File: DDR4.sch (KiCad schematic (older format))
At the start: 4 parts, among them U14 2199155-1

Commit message: Update labels on the schematics
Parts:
- removed R158: R_0R_0603, rdimm-breakout-footprints:0603-res, symbol rdimm-breakout:R_0R_0603-rdimm-breakout
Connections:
- net labels added: VCC2V5
- net labels removed: VDDSPD
- wire segments 409 -> 407
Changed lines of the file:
@@
 Text GLabel 11950 8225 2    50   Input ~ 0
 DQ59
-Text GLabel 11950 8425 2    50   Input ~ 0
-VDDSPD
 Wire Wire Line
 	11225 8425 11950 8425
@@
 Wire Wire Line
 	10225 8225 10225 9000
-Text GLabel 13975 9375 2    50   Input ~ 0
-VDDSPD
-Wire Wire Line
-	13400 9375 13100 9375
-Text GLabel 13100 9375 0    50   Input ~ 0
-VPP
-$Comp
-L rdimm-breakout:R_0R_0603-rdimm-breakout R?
-U 1 1 632B1D0D
-P 13550 9375
-AR Path="/60225B0C/632B1D0D" Ref="R?"  Part="1"
-AR Path="/61827943/632B1D0D" Ref="R158"  Part="1"
-F 0 "R158" H 13500 9475 60  0000 C CNN
-F 1 "R_0R_0603" H 13550 9225 60  0001 C CNN
-F 2 "rdimm-breakout-footprints:0603-res" H 13750 9575 60  0001 L CNN
-F 3 "" H 13550 9375 50  0001 C CNN
-F 4 "BOURNS" H 13750 9775 60  0001 L CNN "Manufacturer"
-F 5 "CR0603-J/-000ELF" H 13750 9675 60  0001 L CNN "MPN"
-F 6 "0R" H 13700 9325 50  0000 C CNN "Val"
-	1    13550 9375
-	1    0    0    -1
-$EndComp
-Wire Wire Line
-	13700 9375 13975 9375
 Text Notes 12325 8450 0    50   ~ 0
 2V5
@@
 Text GLabel 11950 8525 2    50   Input ~ 0
 SDA_2V5
+Text GLabel 11950 8425 2    50   Input ~ 0
+VCC2V5
 $EndSCHEMATC

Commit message: Add initial component placement
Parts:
- removed R157: R_0R_0603, rdimm-breakout-footprints:0603-res, symbol rdimm-breakout:R_0R_0603-rdimm-breakout
- removed TP10: TP_SMD1MM, rdimm-breakout-footprints:Testpoint_smd_1mm, symbol rdimm-breakout:TP_SMD1MM-rdimm-breakout
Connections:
- net labels removed: VIN
- wire segments 407 -> 405
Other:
- note removed: "NVRDIMM Backup voltage"
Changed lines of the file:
@@
 Wire Wire Line
 	5250 2050 4850 2050
-$Comp
-L rdimm-breakout:TP_SMD1MM-rdimm-breakout TP10
-U 1 1 618505E7
-P 2250 1850
-F 0 "TP10" V 2155 1897 50  0000 C CNN
-F 1 "TP_SMD1MM" H 2250 1750 50  0001 C CNN
-F 2 "rdimm-breakout-footprints:Testpoint_smd_1mm" H 2450 2050 60  0001 L CNN
-F 3 "" H 2450 2150 60  0001 L CNN
-	1    2250 1850
-	0    -1   -1   0
-$EndComp
-Text Label 2000 1850 0    50   ~ 0
-12V
-Wire Notes Line
-	1275 1550 1275 2050
-Wire Notes Line
-	1275 2050 2350 2050
-Wire Notes Line
-	2350 2050 2350 1550
-Wire Notes Line
-	2350 1550 1275 1550
-Text Notes 1350 1650 0    50   ~ 0
-NVRDIMM Backup voltage
-$Comp
-L rdimm-breakout:R_0R_0603-rdimm-breakout R157
-U 1 1 61903C55
-P 1800 1850
-F 0 "R157" H 1800 1950 60  0000 C CNN
-F 1 "R_0R_0603" H 1800 1700 60  0001 C CNN
-F 2 "rdimm-breakout-footprints:0603-res" H 2000 2050 60  0001 L CNN
-F 3 "" H 1800 1850 50  0001 C CNN
-F 4 "BOURNS" H 2000 2250 60  0001 L CNN "Manufacturer"
-F 5 "CR0603-J/-000ELF" H 2000 2150 60  0001 L CNN "MPN"
-F 6 "0R" H 1950 1775 50  0000 C CNN "Val"
-F 7 "DNP" H 1800 1850 50  0000 C CNN "DNP"
-	1    1800 1850
-	-1   0    0    1
-$EndComp
-Wire Wire Line
-	2150 1850 1950 1850
-Text GLabel 1550 1850 0    50   Input ~ 0
-VIN
-Wire Wire Line
-	1650 1850 1550 1850
 Text GLabel 3500 2050 0    50   Input ~ 0
 NC

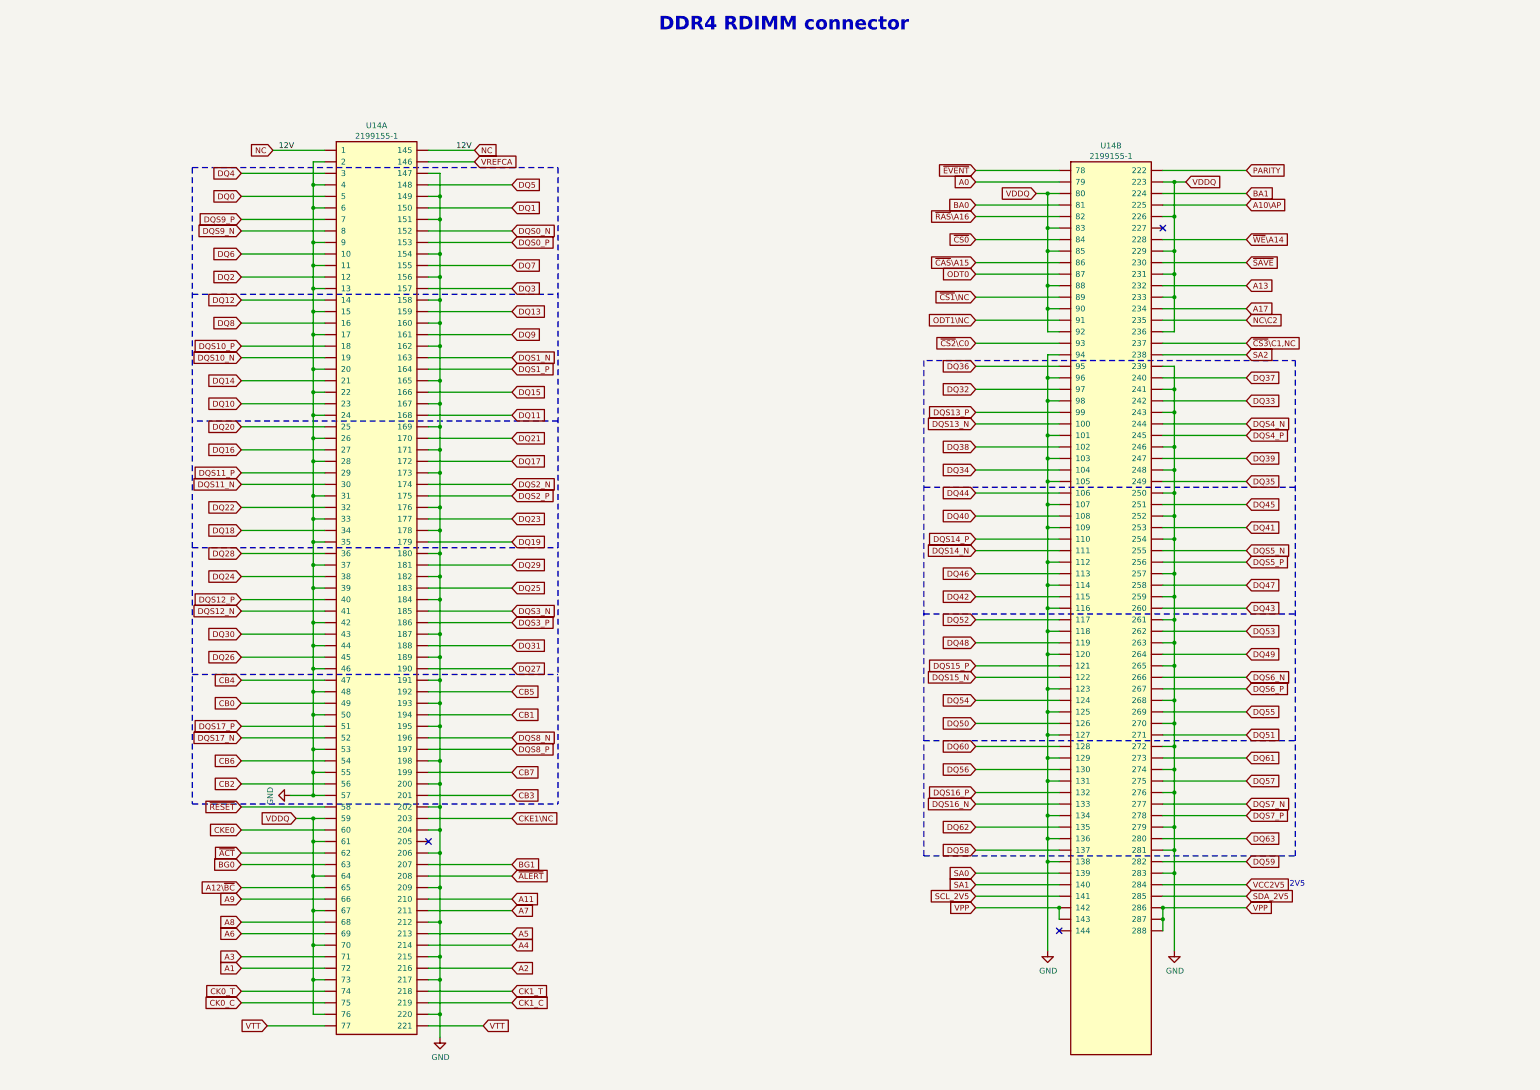
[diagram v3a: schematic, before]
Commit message: Assign MPN to the RDIMM connector
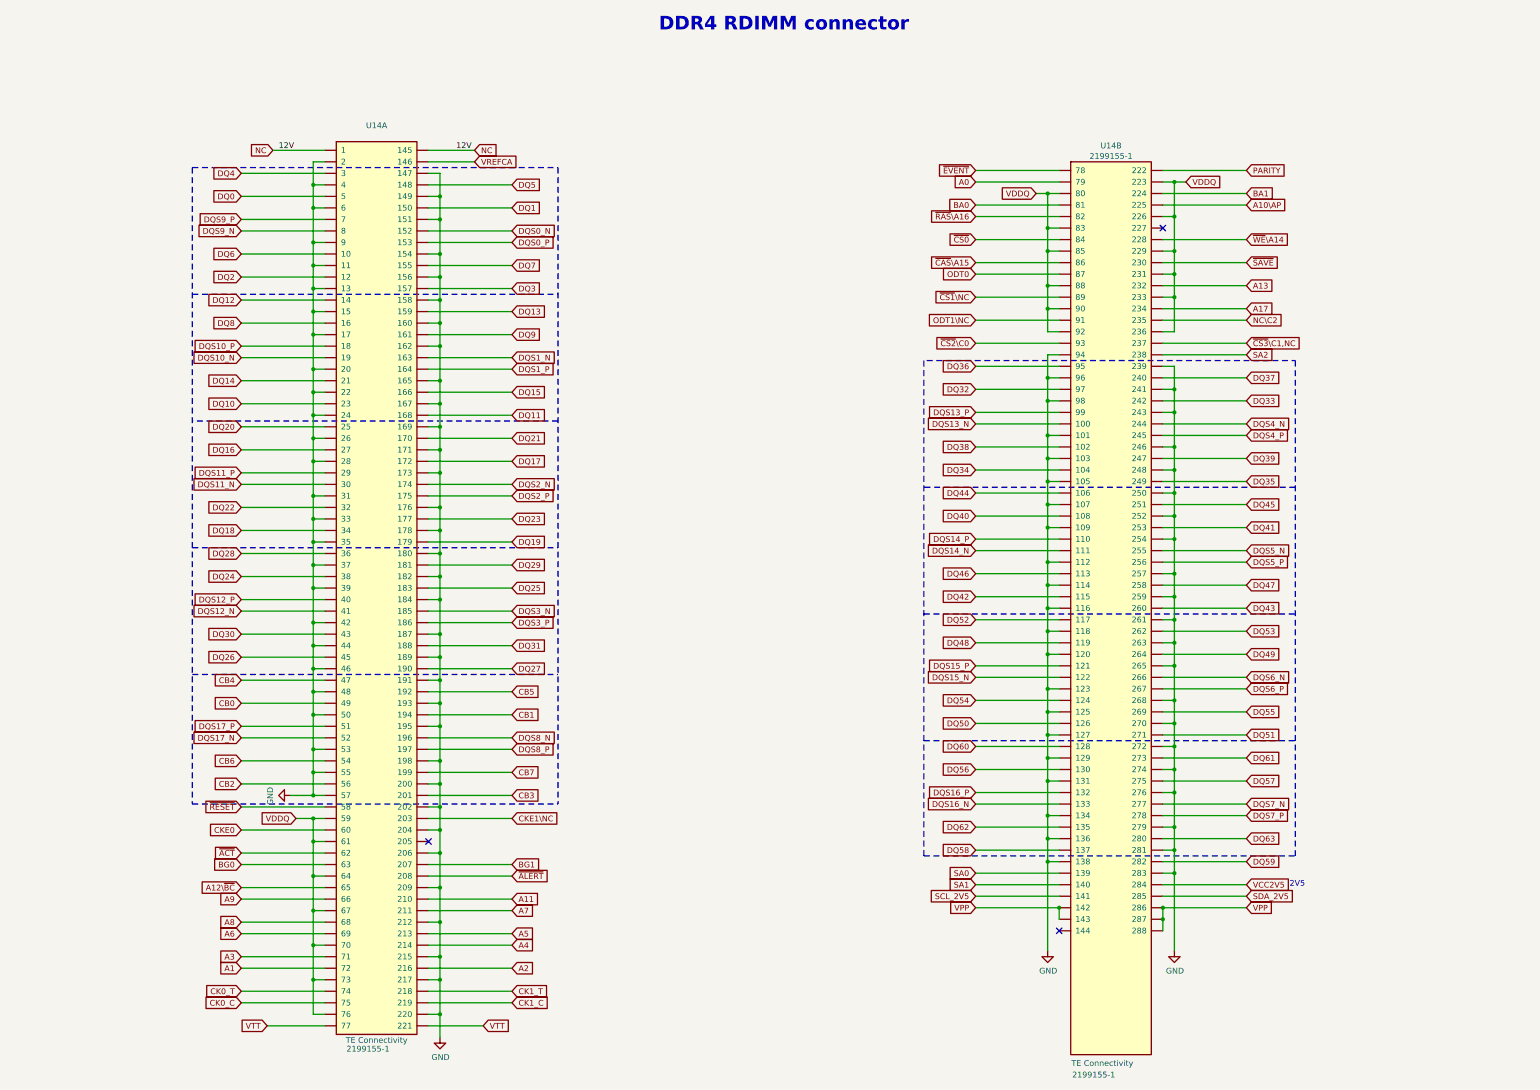
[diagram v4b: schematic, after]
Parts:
- U14: MPN (none) -> 2199155-1; Manufacturer (none) -> TE Connectivity
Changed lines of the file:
@@
 F 1 "2199155-1" H 10775 17649 50  0000 C CNN
 F 2 "rdimm-breakout-footprints:2199155-1" H 9500 16575 50  0001 C CNN
-F 3 "" H 9500 16575 50  0001 C CNN
+F 3 "https://www.te.com/commerce/DocumentDelivery/DDEController?Action=srchrtrv&DocNm=2199155&DocType=Customer+Drawing&DocLang=English" H 9500 16575 50  0001 C CNN
+F 4 "2199155-1" H 10625 9675 50  0000 C CNN "MPN"
+F 5 "TE Connectivity" H 10700 9775 50  0000 C CNN "Manufacturer"
 	2    10175 9875
 	1    0    0    -1
@@
 AR Path="/61827943/61972CDA" Ref="U14"  Part="1"
 F 0 "U14" H 4400 17565 50  0000 C CNN
-F 1 "2199155-1" H 4400 17474 50  0000 C CNN
+F 1 "2199155-1" H 4400 17474 50  0001 C CNN
 F 2 "rdimm-breakout-footprints:2199155-1" H 3125 16400 50  0001 C CNN
-F 3 "" H 3125 16400 50  0001 C CNN
+F 3 "https://www.te.com/commerce/DocumentDelivery/DDEController?Action=srchrtrv&DocNm=2199155&DocType=Customer+Drawing&DocLang=English" H 3125 16400 50  0001 C CNN
+F 4 "2199155-1" H 4325 9550 50  0000 C CNN "MPN"
+F 5 "TE Connectivity" H 4400 9625 50  0000 C CNN "Manufacturer"
 	1    3800 9700
 	1    0    0    -1

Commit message: Update naming convention
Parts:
- U14: footprint rdimm-breakout-footprints:2199155-1 -> ddr4-spd-breakout-footprints:2199155-1; symbol rdimm-breakout:2199155-1-rdimm-breakout -> ddr4-spd-breakout:2199155-1-ddr4-spd-breakout
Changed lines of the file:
@@
 $EndDescr
 $Comp
-L rdimm-breakout:2199155-1-rdimm-breakout U?
+L ddr4-spd-breakout:2199155-1-ddr4-spd-breakout U?
 U 2 1 61972CE0
 P 10175 9875
@@
 F 0 "U14" H 10775 17740 50  0000 C CNN
 F 1 "2199155-1" H 10775 17649 50  0000 C CNN
-F 2 "rdimm-breakout-footprints:2199155-1" H 9500 16575 50  0001 C CNN
+F 2 "ddr4-spd-breakout-footprints:2199155-1" H 9500 16575 50  0001 C CNN
 F 3 "https://www.te.com/commerce/DocumentDelivery/DDEController?Action=srchrtrv&DocNm=2199155&DocType=Customer+Drawing&DocLang=English" H 9500 16575 50  0001 C CNN
 F 4 "2199155-1" H 10625 9675 50  0000 C CNN "MPN"
@@
 	3950 2950 3225 2950
 $Comp
-L rdimm-breakout:2199155-1-rdimm-breakout U?
+L ddr4-spd-breakout:2199155-1-ddr4-spd-breakout U?
 U 1 1 61972CDA
 P 3800 9700
@@
 F 0 "U14" H 4400 17565 50  0000 C CNN
 F 1 "2199155-1" H 4400 17474 50  0001 C CNN
-F 2 "rdimm-breakout-footprints:2199155-1" H 3125 16400 50  0001 C CNN
+F 2 "ddr4-spd-breakout-footprints:2199155-1" H 3125 16400 50  0001 C CNN
 F 3 "https://www.te.com/commerce/DocumentDelivery/DDEController?Action=srchrtrv&DocNm=2199155&DocType=Customer+Drawing&DocLang=English" H 3125 16400 50  0001 C CNN
 F 4 "2199155-1" H 4325 9550 50  0000 C CNN "MPN"
@@
 VDDQ
 $Comp
-L rdimm-breakout:GND-rdimm-breakout #PWR0148
+L ddr4-spd-breakout:GND-ddr4-spd-breakout #PWR0148
 U 1 1 628D8B81
 P 4950 9750
@@
 Connection ~ 4950 7950
 $Comp
-L rdimm-breakout:GND-rdimm-breakout #PWR0150
+L ddr4-spd-breakout:GND-ddr4-spd-breakout #PWR0150
 U 1 1 62DBB5DD
 P 3650 7650
@@
 Connection ~ 3850 7650
 $Comp
-L rdimm-breakout:GND-rdimm-breakout #PWR0204
+L ddr4-spd-breakout:GND-ddr4-spd-breakout #PWR0204
 U 1 1 62FAA504
 P 11325 9000
@@
 	11325 8325 11325 9000
 $Comp
-L rdimm-breakout:GND-rdimm-breakout #PWR0230
+L ddr4-spd-breakout:GND-ddr4-spd-breakout #PWR0230
 U 1 1 6309AE85
 P 10225 9000
